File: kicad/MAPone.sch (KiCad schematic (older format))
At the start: 32 parts, among them J1 BARREL_JACK, J2 USB-Micro, P1 CONN_1, P2 CONN_1, P3 CONN_1, P4 CONN_1, SW1 RST, U1 7805, U2 ATMEGA328-P, X1 16MHz

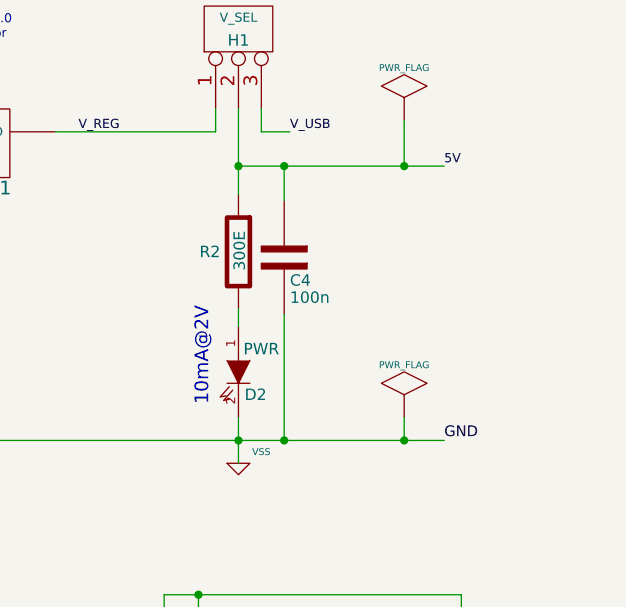
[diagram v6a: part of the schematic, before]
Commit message: MAPone Schematic, PCB, BoM complete. USB<>UART PCB Pending
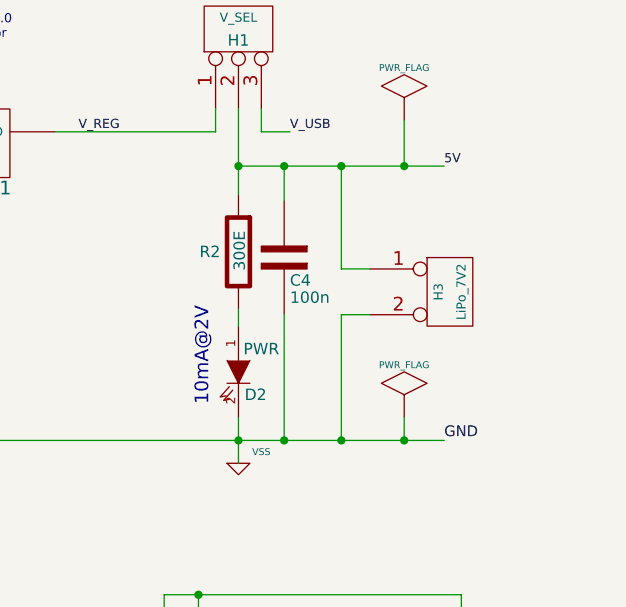
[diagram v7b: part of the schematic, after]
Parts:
- added H3: LiPo_7V2, MAPone.pretty:Pin_Header_Straight_1x02, symbol CONN_2
- C1, C3, C4, C5, C6, C7, C8: footprint Capacitors_SMD:C_0805_HandSoldering -> MAPone.pretty:C_0805_HandSoldering
- C2: footprint Capacitors_Elko_ThroughHole:Elko_vert_11.2x6.3mm_RM2.5 -> MAPone.pretty:Elko_vert_11.2x6.3mm_RM2.5
- D1: footprint Diodes_ThroughHole:Diode_DO-41_SOD81_Vertical_KathodeUp -> MAPone.pretty:Diode_DO-41_SOD81_Vertical_KathodeUp
- D2, D3: footprint LEDs:LED-3MM -> MAPone.pretty:LED-3MM
- H1: footprint uControl:Header_3 -> MAPone.pretty:Header_3
- H2, H4: footprint Socket_Strips:Socket_Strip_Straight_1x06 -> MAPone.pretty:Socket_Strip_Straight_1x06
- H5: footprint uControl:Header_A_REF -> MAPone.pretty:Header_A_REF
- H6, H7: footprint Socket_Strips:Socket_Strip_Straight_1x08 -> MAPone.pretty:Socket_Strip_Straight_1x08
- H8: footprint BADGEr:Header_FTDI -> MAPone.pretty:Header_FTDI
- H9: footprint BADGEr:Header_ICSP -> MAPone.pretty:Header_ICSP
- J1: footprint uControl:JACK_ALIM -> MAPone.pretty:JACK_ALIM
- J2: footprint BADGEr:USB_B_Micro -> MAPone.pretty:USB_B_Micro
- P1, P2, P3, P4: footprint BADGEr:vite_3mm -> MAPone.pretty:vite_3mm
- R1, R2, R3: footprint Resistors_SMD:R_0805_HandSoldering -> MAPone.pretty:R_0805_HandSoldering
- SW1: footprint uControl:SW-PB -> MAPone.pretty:SW-PB
- U1: footprint Discret:LM78XXV -> MAPone.pretty:LM78XXV
- X1: footprint Crystals:Crystal_HC49-U_Vertical_3Pin -> MAPone.pretty:Crystal_HC49-U_Vertical_3Pin
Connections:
- net 5V: now also H3.1 (P1)
- net GND: now also H3.2 (PM)
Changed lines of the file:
@@
 10 84 01 40 0C B0 20 08 82 20 0C 00 62 80 05 41 10 04 61 00 10 03 2C 08 82 20 08 03 80 18 60 41
 10 04 41 18 00 C4 00 0B 82 20 08 C2 00 20 06 58 10 04 41 10 06 80 FF 05 00 29 65 D5 29 35 3D 11
-00 00 00 00 49 45 4E 44 AE 42 60 82 00
+00 00 00 00 49 45 4E 44 AE 42 60 82 59
 EndData
 $EndBitmap
@@
 F 0 "C5" V 1425 4050 50  0000 L CNN
 F 1 "100n" V 1225 3825 50  0000 L CNN
-F 2 "Capacitors_SMD:C_0805_HandSoldering" H 1325 4025 60  0001 C CNN
+F 2 "MAPone.pretty:C_0805_HandSoldering" H 1325 4025 60  0001 C CNN
 F 3 "" H 1325 4025 60  0001 C CNN
 	1    1325 4025
@@
 F 0 "R3" V 5100 6575 50  0000 C CNN
 F 1 "300E" H 5300 6525 50  0000 C CNN
-F 2 "Resistors_SMD:R_0805_HandSoldering" H 5300 6525 60  0001 C CNN
+F 2 "MAPone.pretty:R_0805_HandSoldering" H 5300 6525 60  0001 C CNN
 F 3 "" H 5300 6525 60  0001 C CNN
 	1    5300 6525
@@
 F 0 "D3" V 5425 7175 50  0000 C CNN
 F 1 "Blink" V 5150 7225 50  0000 C CNN
-F 2 "LEDs:LED-3MM" H 5300 7125 60  0001 C CNN
+F 2 "MAPone.pretty:LED-3MM" H 5300 7125 60  0001 C CNN
 F 3 "" H 5300 7125 60  0001 C CNN
 	1    5300 7125
@@
 F 0 "H5" V 650 2725 50  0000 C CNN
 F 1 "AREF" V 750 2725 40  0000 C CNN
-F 2 "uControl:Header_A_REF" H 700 2725 60  0001 C CNN
+F 2 "MAPone.pretty:Header_A_REF" H 700 2725 60  0001 C CNN
 F 3 "" H 700 2725 60  0001 C CNN
 	1    700  2725
@@
 F 0 "H2" V 5125 1775 60  0000 C CNN
 F 1 "Power" V 5225 1775 60  0000 C CNN
-F 2 "Socket_Strips:Socket_Strip_Straight_1x06" H 5175 1825 60  0001 C CNN
+F 2 "MAPone.pretty:Socket_Strip_Straight_1x06" H 5175 1825 60  0001 C CNN
 F 3 "" H 5175 1825 60  0001 C CNN
 	1    5175 1825
@@
 F 0 "H4" V 5125 2675 60  0000 C CNN
 F 1 "ANALOG" V 5225 2675 60  0000 C CNN
-F 2 "Socket_Strips:Socket_Strip_Straight_1x06" H 5175 2675 60  0001 C CNN
+F 2 "MAPone.pretty:Socket_Strip_Straight_1x06" H 5175 2675 60  0001 C CNN
 F 3 "" H 5175 2675 60  0001 C CNN
 	1    5175 2675
@@
 F 0 "H7" V 5125 4575 60  0000 C CNN
 F 1 "IO_H" V 5225 4575 60  0000 C CNN
-F 2 "Socket_Strips:Socket_Strip_Straight_1x08" H 5175 4575 60  0001 C CNN
+F 2 "MAPone.pretty:Socket_Strip_Straight_1x08" H 5175 4575 60  0001 C CNN
 F 3 "" H 5175 4575 60  0001 C CNN
 	1    5175 4575
@@
 F 0 "H6" V 5125 3675 60  0000 C CNN
 F 1 "IO_L" V 5225 3675 60  0000 C CNN
-F 2 "Socket_Strips:Socket_Strip_Straight_1x08" H 5175 3675 60  0001 C CNN
+F 2 "MAPone.pretty:Socket_Strip_Straight_1x08" H 5175 3675 60  0001 C CNN
 F 3 "" H 5175 3675 60  0001 C CNN
 	1    5175 3675
@@
 F 0 "H1" V 9925 950 50  0000 C CNN
 F 1 "V_SEL" V 10025 950 40  0000 C CNN
-F 2 "uControl:Header_3" V 10125 950 40  0001 C CNN
+F 2 "MAPone.pretty:Header_3" V 10125 950 40  0001 C CNN
 F 3 "" H 9975 950 60  0001 C CNN
 	1    9975 950
@@
 F 0 "P2" V 4200 7050 40  0000 L CNN
 F 1 "CONN_1" H 4125 7105 30  0001 C CNN
-F 2 "BADGEr:vite_3mm" H 4125 7050 60  0001 C CNN
+F 2 "MAPone.pretty:vite_3mm" H 4125 7050 60  0001 C CNN
 F 3 "" H 4125 7050 60  0001 C CNN
 	1    4125 7050
@@
 F 0 "P1" V 4000 7050 40  0000 L CNN
 F 1 "CONN_1" H 3925 7105 30  0001 C CNN
-F 2 "BADGEr:vite_3mm" H 3925 7050 60  0001 C CNN
+F 2 "MAPone.pretty:vite_3mm" H 3925 7050 60  0001 C CNN
 F 3 "" H 3925 7050 60  0001 C CNN
 	1    3925 7050
@@
 F 0 "C2" V 8075 1975 50  0000 L CNN
 F 1 "100u" V 8150 1975 50  0000 L CNN
-F 2 "Capacitors_Elko_ThroughHole:Elko_vert_11.2x6.3mm_RM2.5" H 7975 1950 60  0001 C CNN
+F 2 "MAPone.pretty:Elko_vert_11.2x6.3mm_RM2.5" H 7975 1950 60  0001 C CNN
 F 3 "" H 7975 1950 60  0001 C CNN
 	1    7975 1950
@@
 F 0 "R2" V 9975 2050 50  0000 C CNN
 F 1 "300E" H 9980 1920 50  0000 C CNN
-F 2 "Resistors_SMD:R_0805_HandSoldering" H 9975 1925 60  0001 C CNN
+F 2 "MAPone.pretty:R_0805_HandSoldering" H 9975 1925 60  0001 C CNN
 F 3 "" H 9975 1925 60  0001 C CNN
 	1    9975 1925
@@
 F 0 "D2" V 10075 2525 50  0000 C CNN
 F 1 "PWR" V 9875 2550 50  0000 C CNN
-F 2 "LEDs:LED-3MM" H 9975 2450 60  0001 C CNN
+F 2 "MAPone.pretty:LED-3MM" H 9975 2450 60  0001 C CNN
 F 3 "" H 9975 2450 60  0001 C CNN
 	1    9975 2450
@@
 F 0 "C3" V 8225 1850 50  0000 L CNN
 F 1 "100n" V 8150 1750 50  0000 L CNN
-F 2 "Capacitors_SMD:C_0805_HandSoldering" H 8325 1950 60  0001 C CNN
+F 2 "MAPone.pretty:C_0805_HandSoldering" H 8325 1950 60  0001 C CNN
 F 3 "" H 8325 1950 60  0001 C CNN
 	1    8325 1950
@@
 F 0 "U1" H 8925 1254 60  0000 C CNN
 F 1 "7805" H 8675 1650 60  0000 C CNN
-F 2 "Discret:LM78XXV" H 8775 1450 60  0001 C CNN
+F 2 "MAPone.pretty:LM78XXV" H 8775 1450 60  0001 C CNN
 F 3 "" H 8775 1450 60  0001 C CNN
 	1    8775 1450
@@
 F 0 "C4" V 10275 1975 50  0000 L CNN
 F 1 "100n" V 10350 1975 50  0000 L CNN
-F 2 "Capacitors_SMD:C_0805_HandSoldering" H 10175 1950 60  0001 C CNN
+F 2 "MAPone.pretty:C_0805_HandSoldering" H 10175 1950 60  0001 C CNN
 F 3 "" H 10175 1950 60  0001 C CNN
 	1    10175 1950
@@
 F 0 "C6" H 1225 7625 50  0000 L CNN
 F 1 "100n" H 1225 7475 50  0000 L CNN
-F 2 "Capacitors_SMD:C_0805_HandSoldering" H 1125 7550 60  0001 C CNN
+F 2 "MAPone.pretty:C_0805_HandSoldering" H 1125 7550 60  0001 C CNN
 F 3 "" H 1125 7550 60  0001 C CNN
 	1    1125 7550
@@
 F 0 "H8" V 1925 7250 60  0000 C CNN
 F 1 "FTDI" V 2025 7250 60  0000 C CNN
-F 2 "BADGEr:Header_FTDI" H 1975 7250 60  0001 C CNN
+F 2 "MAPone.pretty:Header_FTDI" H 1975 7250 60  0001 C CNN
 F 3 "" H 1975 7250 60  0001 C CNN
 	1    1975 7250
@@
 F 0 "H9" V 3225 7250 60  0000 C CNN
 F 1 "ISP" V 3325 7250 60  0000 C CNN
-F 2 "BADGEr:Header_ICSP" H 3275 7250 60  0001 C CNN
+F 2 "MAPone.pretty:Header_ICSP" H 3275 7250 60  0001 C CNN
 F 3 "" H 3275 7250 60  0001 C CNN
 	1    3275 7250
@@
 F 0 "C1" V 3475 1900 50  0000 L CNN
 F 1 "100n" V 3675 1900 50  0000 L CNN
-F 2 "Capacitors_SMD:C_0805_HandSoldering" H 3575 1875 60  0001 C CNN
+F 2 "MAPone.pretty:C_0805_HandSoldering" H 3575 1875 60  0001 C CNN
 F 3 "" H 3575 1875 60  0001 C CNN
 	1    3575 1875
@@
 F 0 "SW1" H 1875 2775 50  0000 C CNN
 F 1 "RST" H 1875 2625 50  0000 C CNN
-F 2 "uControl:SW-PB" H 1875 2625 60  0001 C CNN
+F 2 "MAPone.pretty:SW-PB" H 1875 2625 60  0001 C CNN
 F 3 "http://industrial.panasonic.com/www-data/pdf/ATK0000/ATK0000CE32.pdf" H 1875 2625 60  0001 C CNN
 F 4 "P10884S-ND" H 1875 2625 60  0001 C CNN "DigiKey"
@@
 F 0 "R1" H 1925 1375 50  0000 C CNN
 F 1 "10k" H 1925 1475 50  0000 C CNN
-F 2 "Resistors_SMD:R_0805_HandSoldering" H 1925 1475 60  0001 C CNN
+F 2 "MAPone.pretty:R_0805_HandSoldering" H 1925 1475 60  0001 C CNN
 F 3 "" H 1925 1475 60  0001 C CNN
 	1    1925 1475
@@
 F 0 "X1" H 1975 3475 60  0000 C CNN
 F 1 "16MHz" H 2125 3150 60  0000 C CNN
-F 2 "Crystals:Crystal_HC49-U_Vertical_3Pin" H 1975 3325 60  0001 C CNN
+F 2 "MAPone.pretty:Crystal_HC49-U_Vertical_3Pin" H 1975 3325 60  0001 C CNN
 F 3 "http://search.murata.co.jp/Ceramy/image/img/w_hinm/L0430E.pdf" H 1975 3325 60  0001 C CNN
 F 4 "490-1214-ND" H 1975 3325 60  0001 C CNN "DigiKey"
@@
 F 0 "D1" H 7675 1250 50  0000 C CNN
 F 1 "1N4007" H 7675 1550 50  0000 C CNN
-F 2 "Diodes_ThroughHole:Diode_DO-41_SOD81_Vertical_KathodeUp" H 7745 1400 60  0001 C CNN
+F 2 "MAPone.pretty:Diode_DO-41_SOD81_Vertical_KathodeUp" H 7745 1400 60  0001 C CNN
 F 3 "" H 7745 1400 60  0000 C CNN
 	1    7675 1400
@@
 F 0 "J1" H 6925 2200 60  0000 C CNN
 F 1 "BARREL_JACK" H 6925 1750 60  0000 C CNN
-F 2 "uControl:JACK_ALIM" H 6925 1950 60  0001 C CNN
+F 2 "MAPone.pretty:JACK_ALIM" H 6925 1950 60  0001 C CNN
 F 3 "" H 6925 1950 60  0000 C CNN
 	1    6925 1950
@@
 F 0 "J2" H 9375 4025 60  0000 C CNN
 F 1 "USB-Micro" H 9225 4150 60  0000 C CNN
-F 2 "BADGEr:USB_B_Micro" H 9950 4100 60  0001 C CNN
+F 2 "MAPone.pretty:USB_B_Micro" H 9950 4100 60  0001 C CNN
 F 3 "" H 9950 4100 60  0000 C CNN
 	1    9950 4100
@@
 F 0 "P3" V 4400 7050 40  0000 L CNN
 F 1 "CONN_1" H 4325 7105 30  0001 C CNN
-F 2 "BADGEr:vite_3mm" H 4325 7050 60  0001 C CNN
+F 2 "MAPone.pretty:vite_3mm" H 4325 7050 60  0001 C CNN
 F 3 "" H 4325 7050 60  0001 C CNN
 	1    4325 7050
@@
 F 0 "P4" V 4600 7050 40  0000 L CNN
 F 1 "CONN_1" H 4525 7105 30  0001 C CNN
-F 2 "BADGEr:vite_3mm" H 4525 7050 60  0001 C CNN
+F 2 "MAPone.pretty:vite_3mm" H 4525 7050 60  0001 C CNN
 F 3 "" H 4525 7050 60  0001 C CNN
 	1    4525 7050
@@
 F 0 "C7" V 1725 4050 50  0000 L CNN
 F 1 "22pF" V 1525 3825 50  0000 L CNN
-F 2 "Capacitors_SMD:C_0805_HandSoldering" H 1625 4025 60  0001 C CNN
+F 2 "MAPone.pretty:C_0805_HandSoldering" H 1625 4025 60  0001 C CNN
 F 3 "" H 1625 4025 60  0001 C CNN
 	1    1625 4025
@@
 F 0 "C8" V 2425 4050 50  0000 L CNN
 F 1 "22pF" V 2225 3825 50  0000 L CNN
-F 2 "Capacitors_SMD:C_0805_HandSoldering" H 2325 4025 60  0001 C CNN
+F 2 "MAPone.pretty:C_0805_HandSoldering" H 2325 4025 60  0001 C CNN
 F 3 "" H 2325 4025 60  0001 C CNN
 	1    2325 4025
@@
 Text Notes 5150 7300 1    60   ~ 0
 10mA@2V2
+$Comp
+L CONN_2 H3
+U 1 1 547AD762
+P 10900 2100
+F 0 "H3" V 10850 2100 40  0000 C CNN
+F 1 "LiPo_7V2" V 10950 2100 40  0000 C CNN
+F 2 "MAPone.pretty:Pin_Header_Straight_1x02" H 10900 2100 60  0001 C CNN
+F 3 "" H 10900 2100 60  0000 C CNN
+	1    10900 2100
+	1    0    0    -1
+$EndComp
+Wire Wire Line
+	10550 2000 10425 2000
+Wire Wire Line
+	10425 2000 10425 1550
+Connection ~ 10425 1550
+Wire Wire Line
+	10550 2200 10425 2200
+Wire Wire Line
+	10425 2200 10425 2750
+Connection ~ 10425 2750
 $EndSCHEMATC

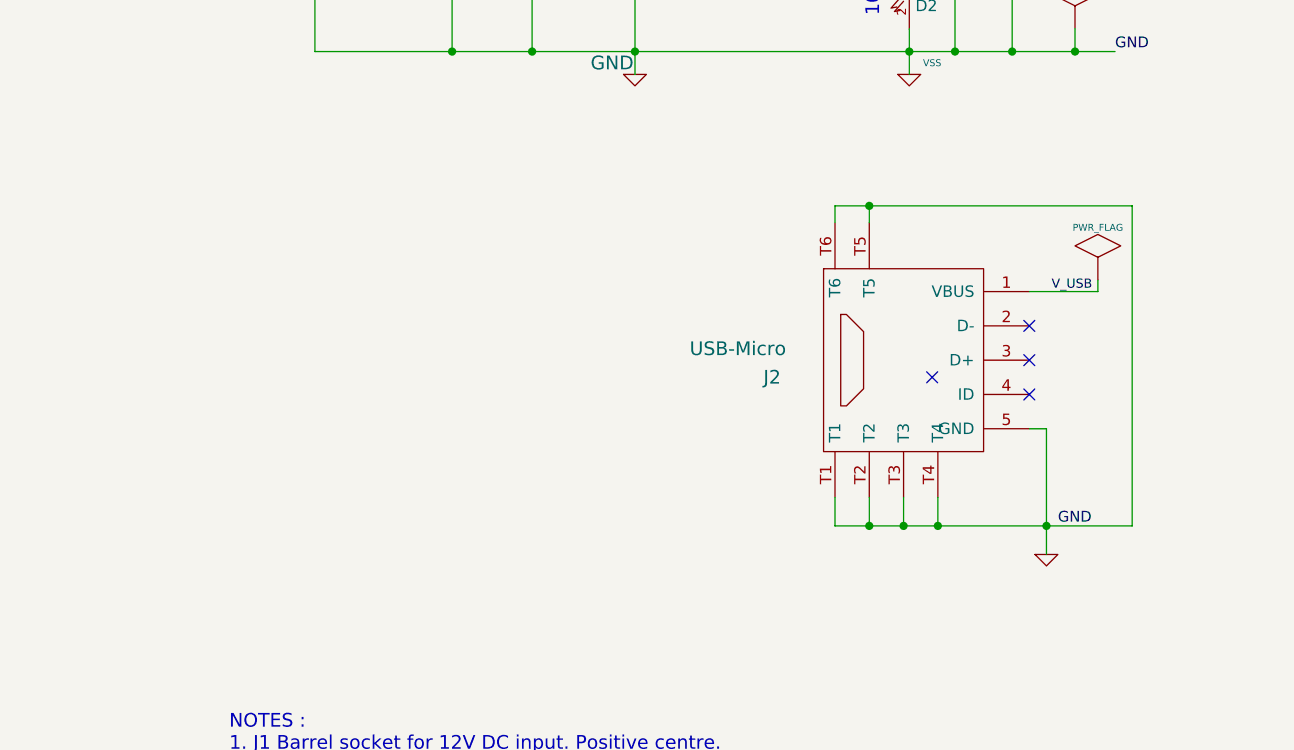
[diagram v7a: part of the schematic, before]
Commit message: MAPone Schematic, PCB, BoM complete. USB<>UART PCB work in progress
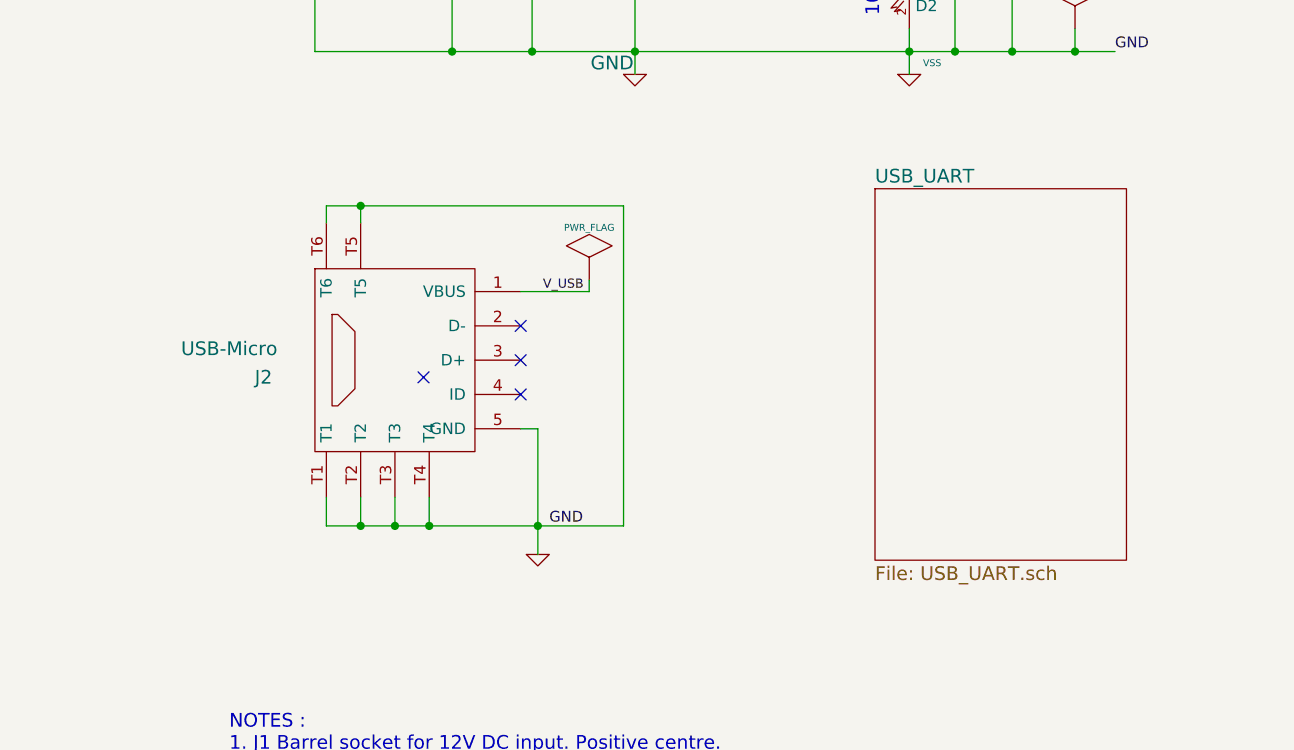
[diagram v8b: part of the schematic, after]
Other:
- moved on the sheet: J2
